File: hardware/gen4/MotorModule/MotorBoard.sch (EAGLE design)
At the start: 66 parts, among them IC1 XMEGA16A4A, M1O1 TEST_PT, M1O2 TEST_PT, M1O3 TEST_PT

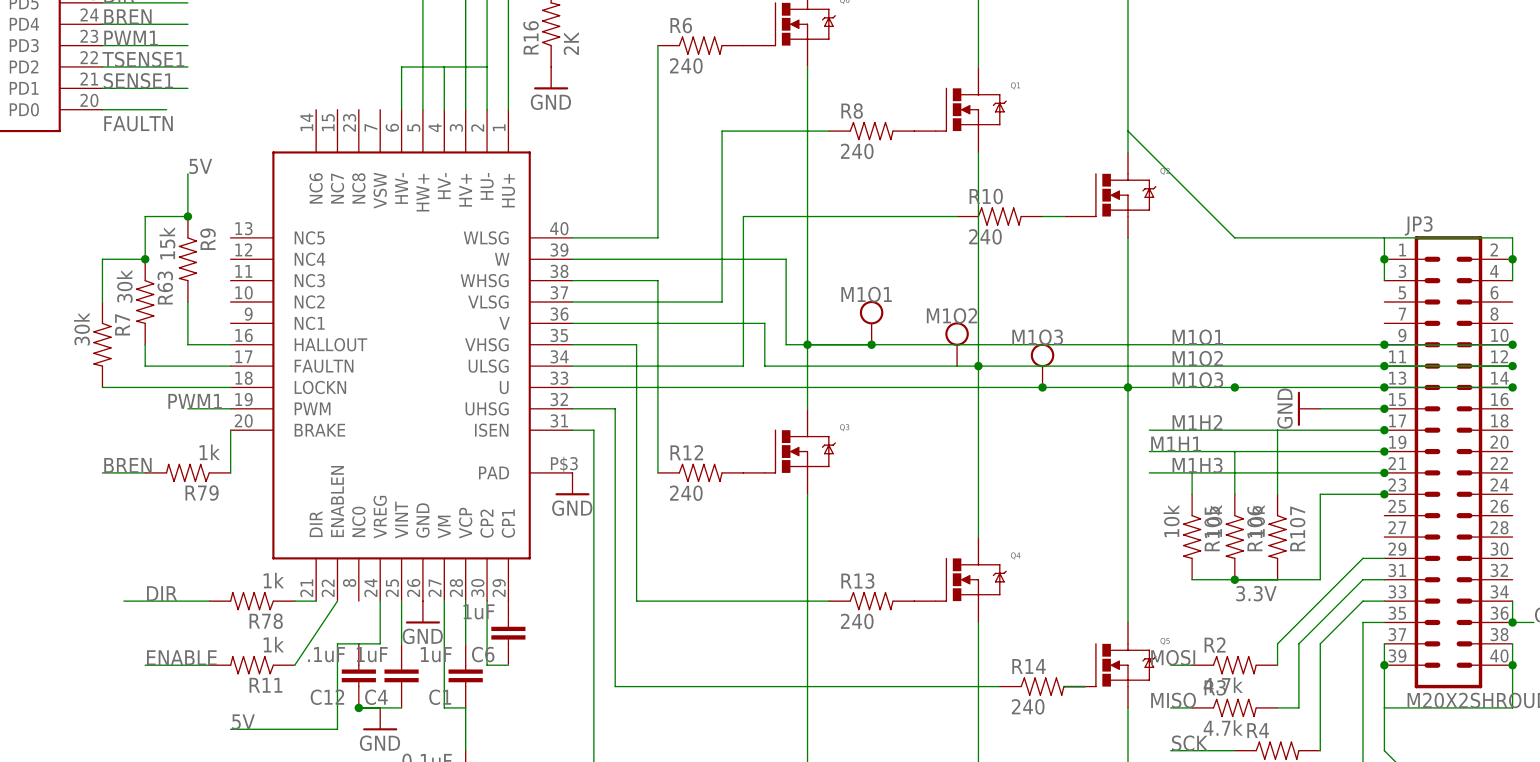
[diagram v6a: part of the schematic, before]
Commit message: fixed up motor board a bit more
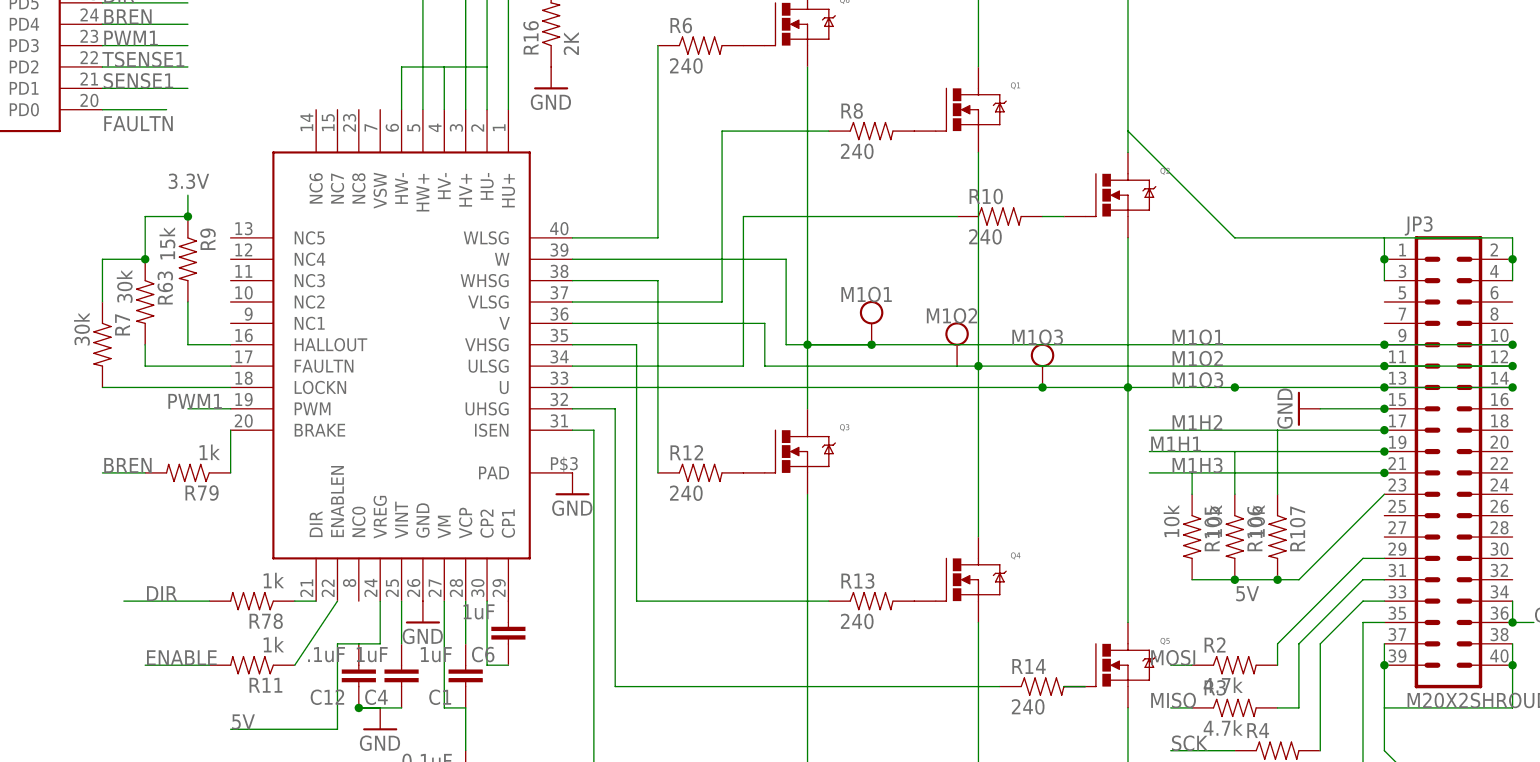
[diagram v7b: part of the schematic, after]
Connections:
- net 3.3V: now also R63.1, R7.1, R9.1; no longer JP3.23, R105.2, R106.2, R107.2
- net 5V: now also JP3.23, R105.2, R106.2, R107.2; no longer R63.1, R7.1, R9.1
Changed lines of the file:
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@@
 <text x="78.74" y="33.02" size="1.778" layer="95">DIR</text>
 <text x="88.9" y="17.78" size="1.778" layer="95">5V</text>
-<text x="83.82" y="83.82" size="1.778" layer="95">5V</text>
 <text x="127" y="116.84" size="1.778" layer="95">5V</text>
+<text x="208.28" y="33.02" size="1.778" layer="95">5V</text>
 </plain>
 <instances>
@@
 <label x="12.7" y="142.24" size="1.778" layer="95"/>
 <label x="228.6" y="142.24" size="1.778" layer="95"/>
+<label x="86.36" y="83.82" size="1.778" layer="95" rot="R180"/>
 </segment>
 <segment>
@@
 </segment>
 <segment>
-<pinref part="R105" gate="G$1" pin="2"/>
-<pinref part="R106" gate="G$1" pin="2"/>
-<wire x1="203.2" y1="35.56" x2="208.28" y2="35.56" width="0.1524" layer="91"/>
-<pinref part="R107" gate="G$1" pin="2"/>
-<wire x1="208.28" y1="35.56" x2="213.36" y2="35.56" width="0.1524" layer="91"/>
-<junction x="208.28" y="35.56"/>
-<label x="208.28" y="33.02" size="1.778" layer="95"/>
-<wire x1="218.44" y1="45.72" x2="218.44" y2="35.56" width="0.1524" layer="91"/>
-<wire x1="218.44" y1="35.56" x2="208.28" y2="35.56" width="0.1524" layer="91"/>
-<pinref part="JP3" gate="G$1" pin="23"/>
-<wire x1="218.44" y1="45.72" x2="226.06" y2="45.72" width="0.1524" layer="91"/>
-<junction x="226.06" y="45.72"/>
-</segment>
-<segment>
 <wire x1="228.6" y1="142.24" x2="233.68" y2="142.24" width="0.1524" layer="91"/>
 <pinref part="JP4" gate="G$1" pin="1"/>
@@
 <pinref part="JP2" gate="A" pin="2"/>
 <junction x="33.02" y="73.66"/>
+</segment>
+<segment>
+<pinref part="R7" gate="G$1" pin="1"/>
+<pinref part="R63" gate="G$1" pin="1"/>
+<wire x1="73.66" y1="68.58" x2="73.66" y2="73.66" width="0.1524" layer="91"/>
+<wire x1="73.66" y1="73.66" x2="78.74" y2="73.66" width="0.1524" layer="91"/>
+<pinref part="R9" gate="G$1" pin="1"/>
+<wire x1="78.74" y1="73.66" x2="78.74" y2="78.74" width="0.1524" layer="91"/>
+<wire x1="78.74" y1="78.74" x2="83.82" y2="78.74" width="0.1524" layer="91"/>
+<junction x="78.74" y="73.66"/>
+<wire x1="83.82" y1="78.74" x2="83.82" y2="81.28" width="0.1524" layer="91"/>
+<junction x="83.82" y="78.74"/>
 </segment>
 </net>
@@
 </segment>
 <segment>
-<pinref part="R7" gate="G$1" pin="1"/>
-<pinref part="R63" gate="G$1" pin="1"/>
-<wire x1="73.66" y1="68.58" x2="73.66" y2="73.66" width="0.1524" layer="91"/>
-<wire x1="73.66" y1="73.66" x2="78.74" y2="73.66" width="0.1524" layer="91"/>
-<pinref part="R9" gate="G$1" pin="1"/>
-<wire x1="78.74" y1="73.66" x2="78.74" y2="78.74" width="0.1524" layer="91"/>
-<wire x1="78.74" y1="78.74" x2="83.82" y2="78.74" width="0.1524" layer="91"/>
-<junction x="78.74" y="73.66"/>
-<wire x1="83.82" y1="78.74" x2="83.82" y2="83.82" width="0.1524" layer="91"/>
-<junction x="83.82" y="78.74"/>
-</segment>
-<segment>
 <pinref part="R17" gate="G$1" pin="2"/>
 <wire x1="127" y1="116.84" x2="129.54" y2="116.84" width="0.1524" layer="91"/>
 </segment>
-</net>
+<segment>
+<pinref part="R105" gate="G$1" pin="2"/>
+<pinref part="R106" gate="G$1" pin="2"/>
+<wire x1="203.2" y1="35.56" x2="208.28" y2="35.56" width="0.1524" layer="91"/>
+<pinref part="R107" gate="G$1" pin="2"/>
+<wire x1="208.28" y1="35.56" x2="213.36" y2="35.56" width="0.1524" layer="91"/>
+<junction x="208.28" y="35.56"/>
+<pinref part="JP3" gate="G$1" pin="23"/>
+<wire x1="213.36" y1="35.56" x2="215.9" y2="35.56" width="0.1524" layer="91"/>
+<wire x1="215.9" y1="35.56" x2="226.06" y2="45.72" width="0.1524" layer="91"/>
+<junction x="213.36" y="35.56"/>
+</segment>
+</net>

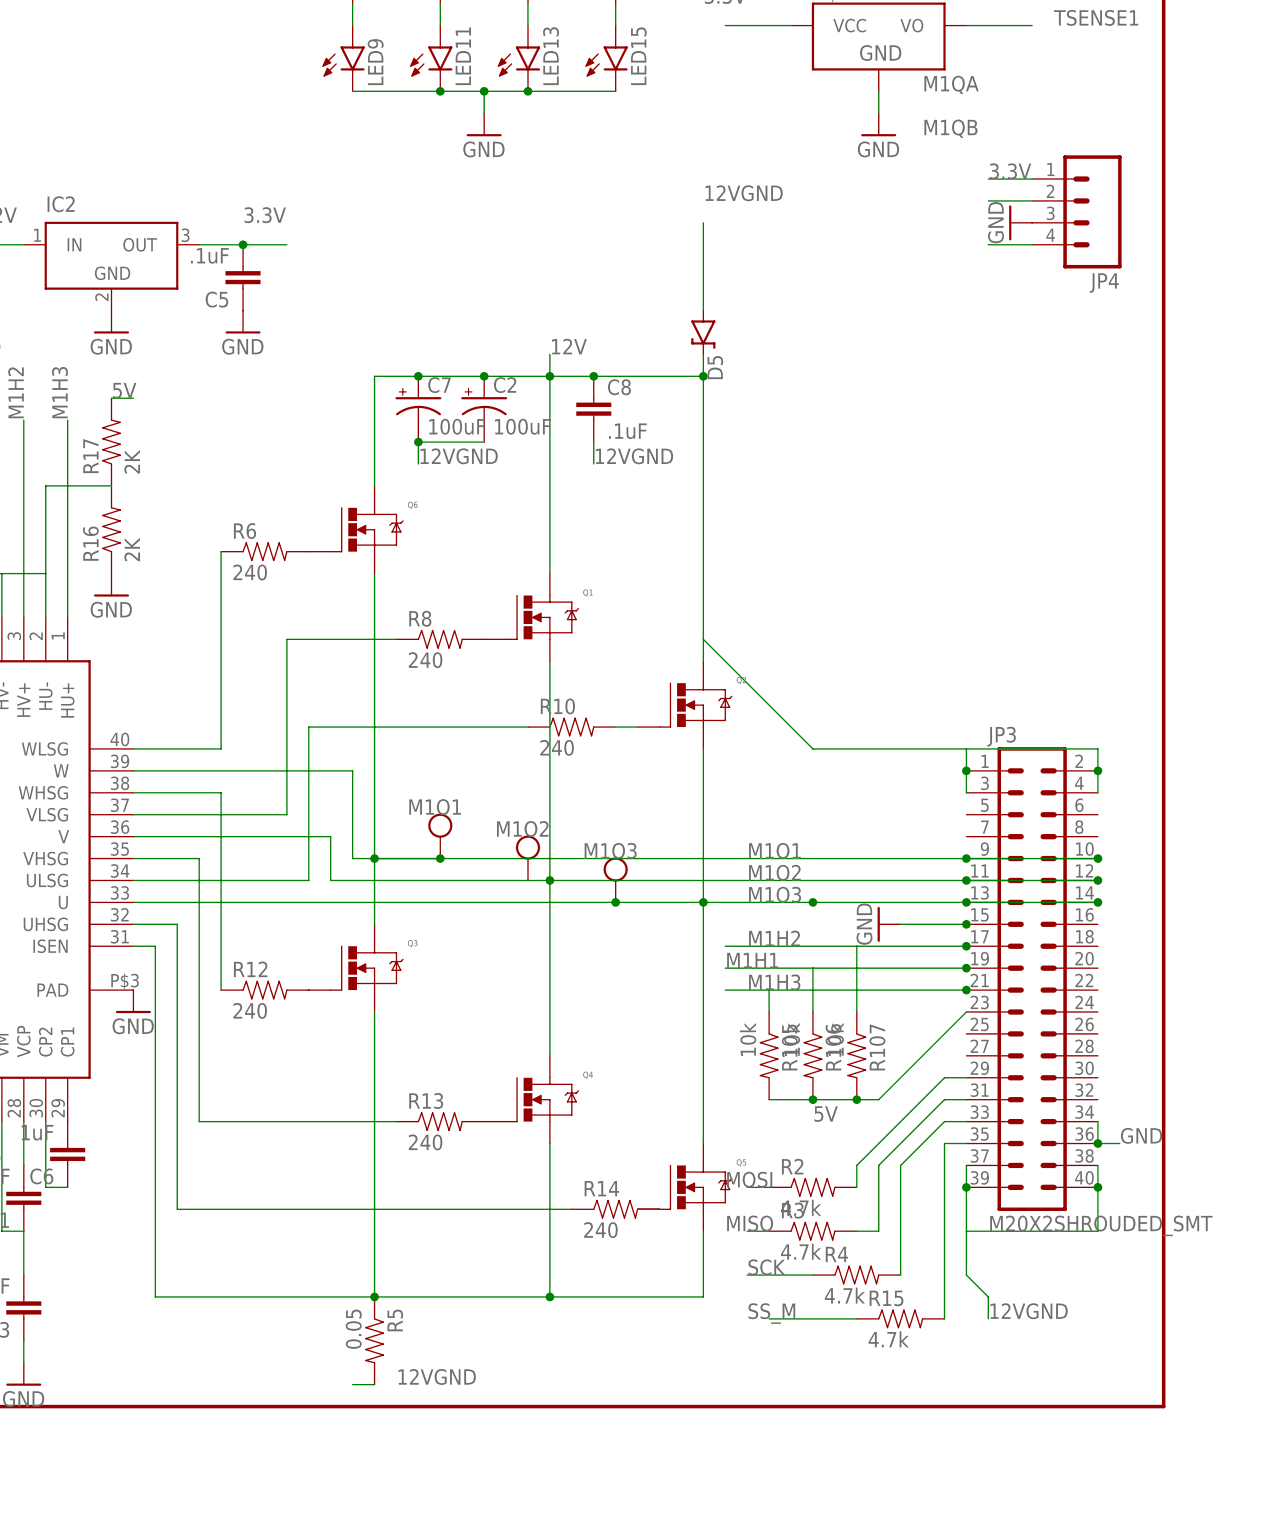
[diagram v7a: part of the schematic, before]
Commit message: motor board fixes
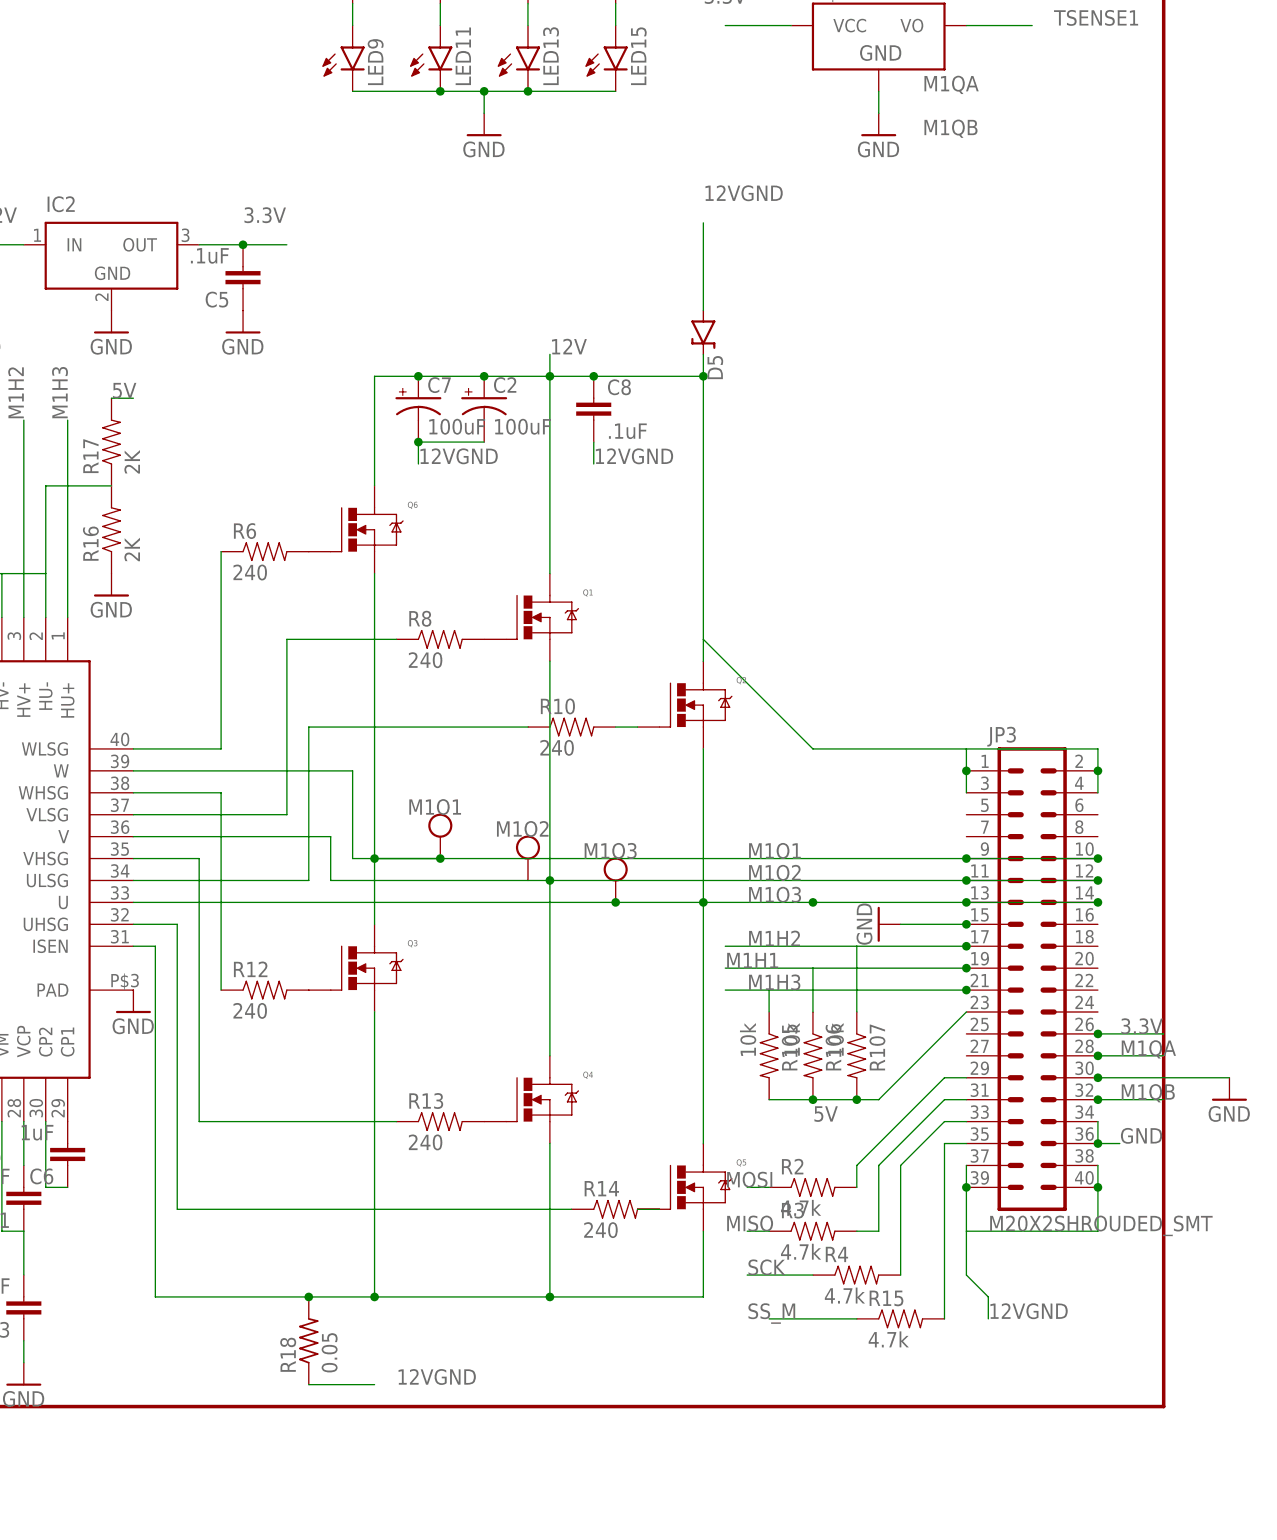
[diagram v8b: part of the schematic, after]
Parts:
- removed JP4: (no value), SparkFun-Connectors:M04SMD_RA_FEMALE
- removed R5: 0.05, SparkFun-Resistors:RESISTOR0805-RES
- added R18: 0.05, resistor:R-US_R2512
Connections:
- net 12VGND: now also R18.1; no longer R5.2
- net 3.3V: now also JP3.26; no longer JP4.1
- net GND: now also JP3.30; no longer JP4.3
- net M1QA: now also JP3.28; no longer JP4.2
- net M1QB: now also JP3.32; no longer JP4.4
- net O1: now also R18.2; no longer R5.1
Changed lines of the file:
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@@
 <part name="C13" library="SparkFun-Passives" deviceset="CAP" device="0805" value="0.1uF"/>
 <part name="GND12" library="SparkFun-Aesthetics" deviceset="GND" device=""/>
-<part name="R5" library="SparkFun-Resistors" deviceset="RESISTOR" device="0805-RES" value="0.05"/>
 <part name="R7" library="SparkFun-Resistors" deviceset="RESISTOR" device="0805-RES" value="30k"/>
 <part name="R9" library="SparkFun-Resistors" deviceset="RESISTOR" device="0805-RES" value="15k"/>
@@
 <part name="GND10" library="SparkFun-Aesthetics" deviceset="GND" device=""/>
 <part name="GND14" library="SparkFun-Aesthetics" deviceset="GND" device=""/>
-<part name="JP4" library="SparkFun-Connectors" deviceset="M04" device="SMD_RA_FEMALE"/>
 <part name="U$1" library="texas2" deviceset="DRV8307" device=""/>
 <part name="C3" library="SparkFun-Capacitors" deviceset="CAP" device="0805" value=".1uF"/>
@@
 <part name="GND16" library="SparkFun-Aesthetics" deviceset="GND" device=""/>
 <part name="JP2" library="pinhead" deviceset="PINHD-2X3" device=""/>
+<part name="R18" library="resistor" deviceset="R-US_" device="R2512" value="0.05"/>
 </parts>
 <sheets>
@@
 <instance part="C13" gate="G$1" x="116.84" y="12.7" rot="R180"/>
 <instance part="GND12" gate="1" x="129.54" y="45.72"/>
-<instance part="R5" gate="G$1" x="157.48" y="7.62" rot="R270"/>
 <instance part="R7" gate="G$1" x="73.66" y="63.5" rot="R270"/>
 <instance part="R9" gate="G$1" x="83.82" y="73.66" rot="R270"/>
@@
 <instance part="S2" gate="S" x="12.7" y="182.88"/>
 <instance part="GND10" gate="1" x="215.9" y="55.88" rot="R270"/>
-<instance part="GND14" gate="1" x="231.14" y="137.16" rot="R270"/>
-<instance part="JP4" gate="G$1" x="238.76" y="139.7" rot="R180"/>
+<instance part="GND14" gate="1" x="256.54" y="35.56"/>
 <instance part="U$1" gate="G$1" x="86.36" y="86.36" rot="R270"/>
 <instance part="C3" gate="G$1" x="111.76" y="132.08" rot="R180"/>
@@
 <instance part="GND16" gate="1" x="142.24" y="124.46"/>
 <instance part="JP2" gate="A" x="27.94" y="71.12"/>
+<instance part="R18" gate="G$1" x="149.86" y="7.62" rot="R90"/>
 </instances>
 <busses>
@@
 <segment>
 <pinref part="GND14" gate="1" pin="GND"/>
-<pinref part="JP4" gate="G$1" pin="3"/>
+<wire x1="256.54" y1="38.1" x2="241.3" y2="38.1" width="0.1524" layer="91"/>
+<pinref part="JP3" gate="G$1" pin="30"/>
+<junction x="241.3" y="38.1"/>
 </segment>
 <segment>
@@
 </segment>
 <segment>
-<pinref part="R5" gate="G$1" pin="2"/>
-<wire x1="157.48" y1="2.54" x2="154.94" y2="2.54" width="0.1524" layer="91"/>
+<pinref part="R18" gate="G$1" pin="1"/>
+<wire x1="157.48" y1="2.54" x2="149.86" y2="2.54" width="0.1524" layer="91"/>
 </segment>
 </net>
@@
 <segment>
 <label x="220.98" y="147.32" size="1.778" layer="95"/>
-<wire x1="228.6" y1="134.62" x2="233.68" y2="134.62" width="0.1524" layer="91"/>
-<pinref part="JP4" gate="G$1" pin="4"/>
+<wire x1="241.3" y1="35.56" x2="248.92" y2="35.56" width="0.1524" layer="91"/>
+<label x="243.84" y="35.56" size="1.778" layer="95"/>
+<pinref part="JP3" gate="G$1" pin="32"/>
+<junction x="241.3" y="35.56"/>
 </segment>
 <segment>
@@
 <segment>
 <label x="220.98" y="152.4" size="1.778" layer="95"/>
-<wire x1="228.6" y1="139.7" x2="233.68" y2="139.7" width="0.1524" layer="91"/>
-<pinref part="JP4" gate="G$1" pin="2"/>
+<wire x1="241.3" y1="40.64" x2="248.92" y2="40.64" width="0.1524" layer="91"/>
+<label x="243.84" y="40.64" size="1.778" layer="95"/>
+<pinref part="JP3" gate="G$1" pin="28"/>
+<junction x="241.3" y="40.64"/>
 </segment>
 <segment>
@@
 <wire x1="177.8" y1="12.7" x2="195.58" y2="12.7" width="0.1524" layer="91"/>
 <junction x="177.8" y="12.7"/>
-<pinref part="R5" gate="G$1" pin="1"/>
 <junction x="157.48" y="12.7"/>
 <wire x1="132.08" y1="12.7" x2="132.08" y2="53.34" width="0.1524" layer="91"/>
 <wire x1="132.08" y1="53.34" x2="129.54" y2="53.34" width="0.1524" layer="91"/>
 <pinref part="U$1" gate="G$1" pin="ISEN"/>
-<wire x1="132.08" y1="12.7" x2="157.48" y2="12.7" width="0.1524" layer="91"/>
+<wire x1="132.08" y1="12.7" x2="149.86" y2="12.7" width="0.1524" layer="91"/>
+<pinref part="R18" gate="G$1" pin="2"/>
+<wire x1="149.86" y1="12.7" x2="157.48" y2="12.7" width="0.1524" layer="91"/>
+<junction x="149.86" y="12.7"/>
 </segment>
 </net>
@@
 <label x="142.24" y="137.16" size="1.778" layer="95"/>
 <label x="12.7" y="142.24" size="1.778" layer="95"/>
-<label x="228.6" y="142.24" size="1.778" layer="95"/>
+<label x="243.84" y="43.18" size="1.778" layer="95"/>
 <label x="86.36" y="83.82" size="1.778" layer="95" rot="R180"/>
 </segment>
@@
 </segment>
 <segment>
-<wire x1="228.6" y1="142.24" x2="233.68" y2="142.24" width="0.1524" layer="91"/>
-<pinref part="JP4" gate="G$1" pin="1"/>
-</segment>
-<segment>
+<wire x1="241.3" y1="43.18" x2="248.92" y2="43.18" width="0.1524" layer="91"/>
+<pinref part="JP3" gate="G$1" pin="26"/>
+<junction x="241.3" y="43.18"/>
+</segment>
+<segment>
